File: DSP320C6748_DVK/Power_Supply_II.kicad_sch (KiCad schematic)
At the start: 46 parts, among them IC8 TPS650250RHBR

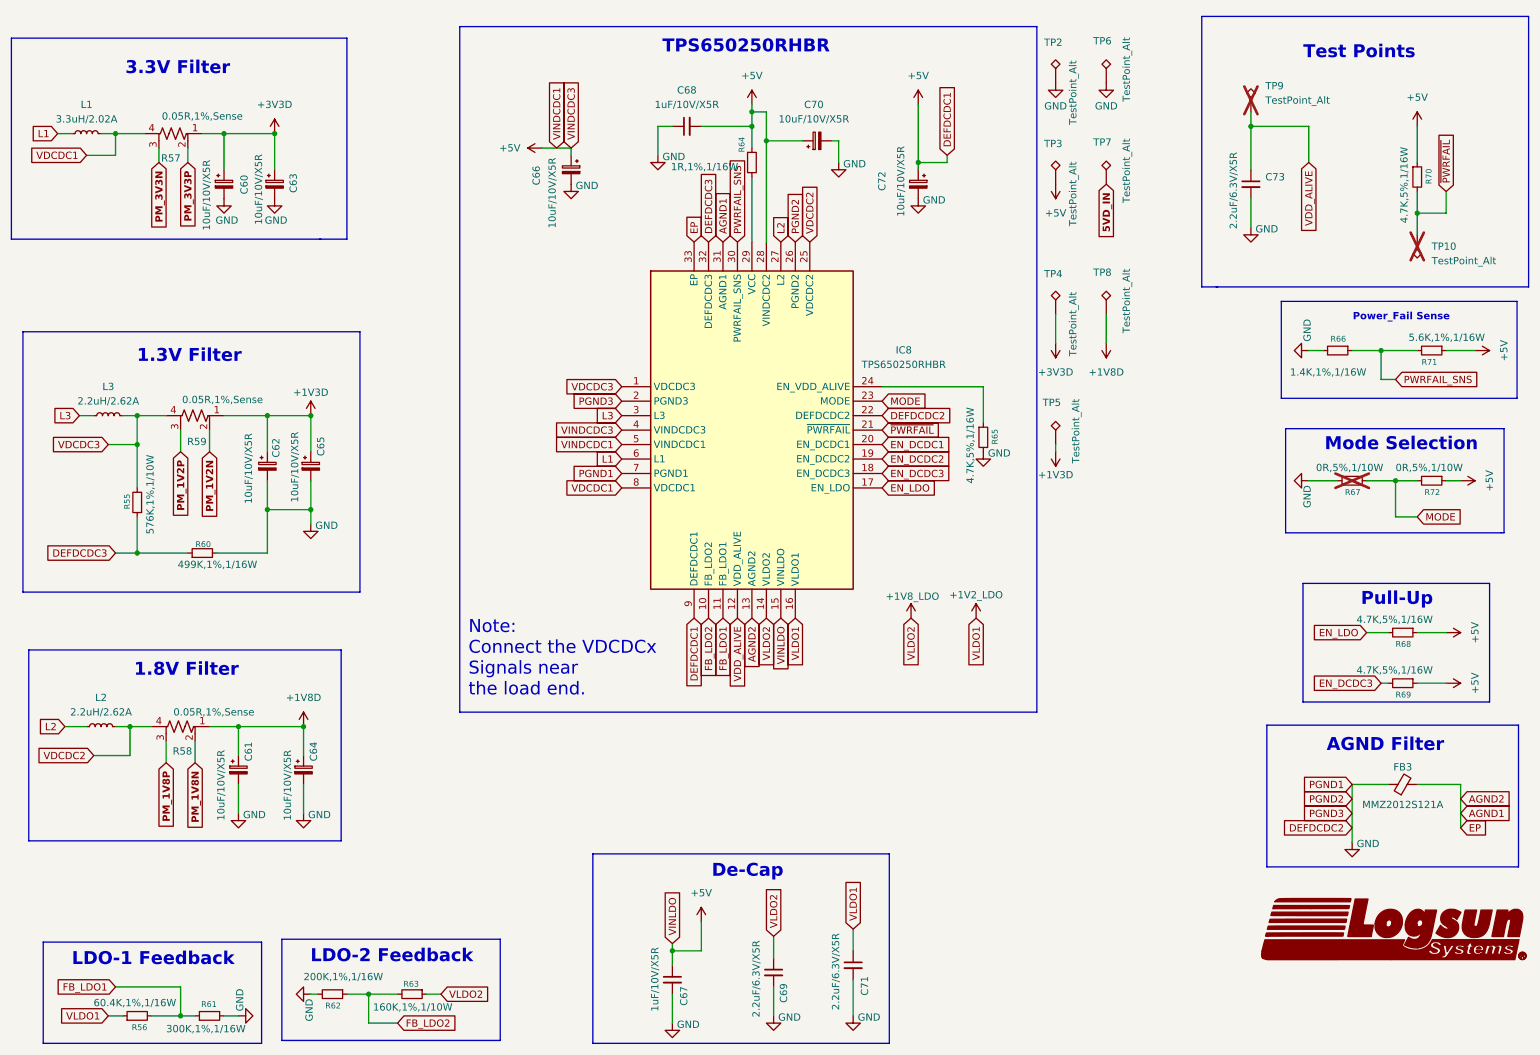
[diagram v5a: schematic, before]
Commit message: Scheamtic Re-annotation done, Some footprints assigned
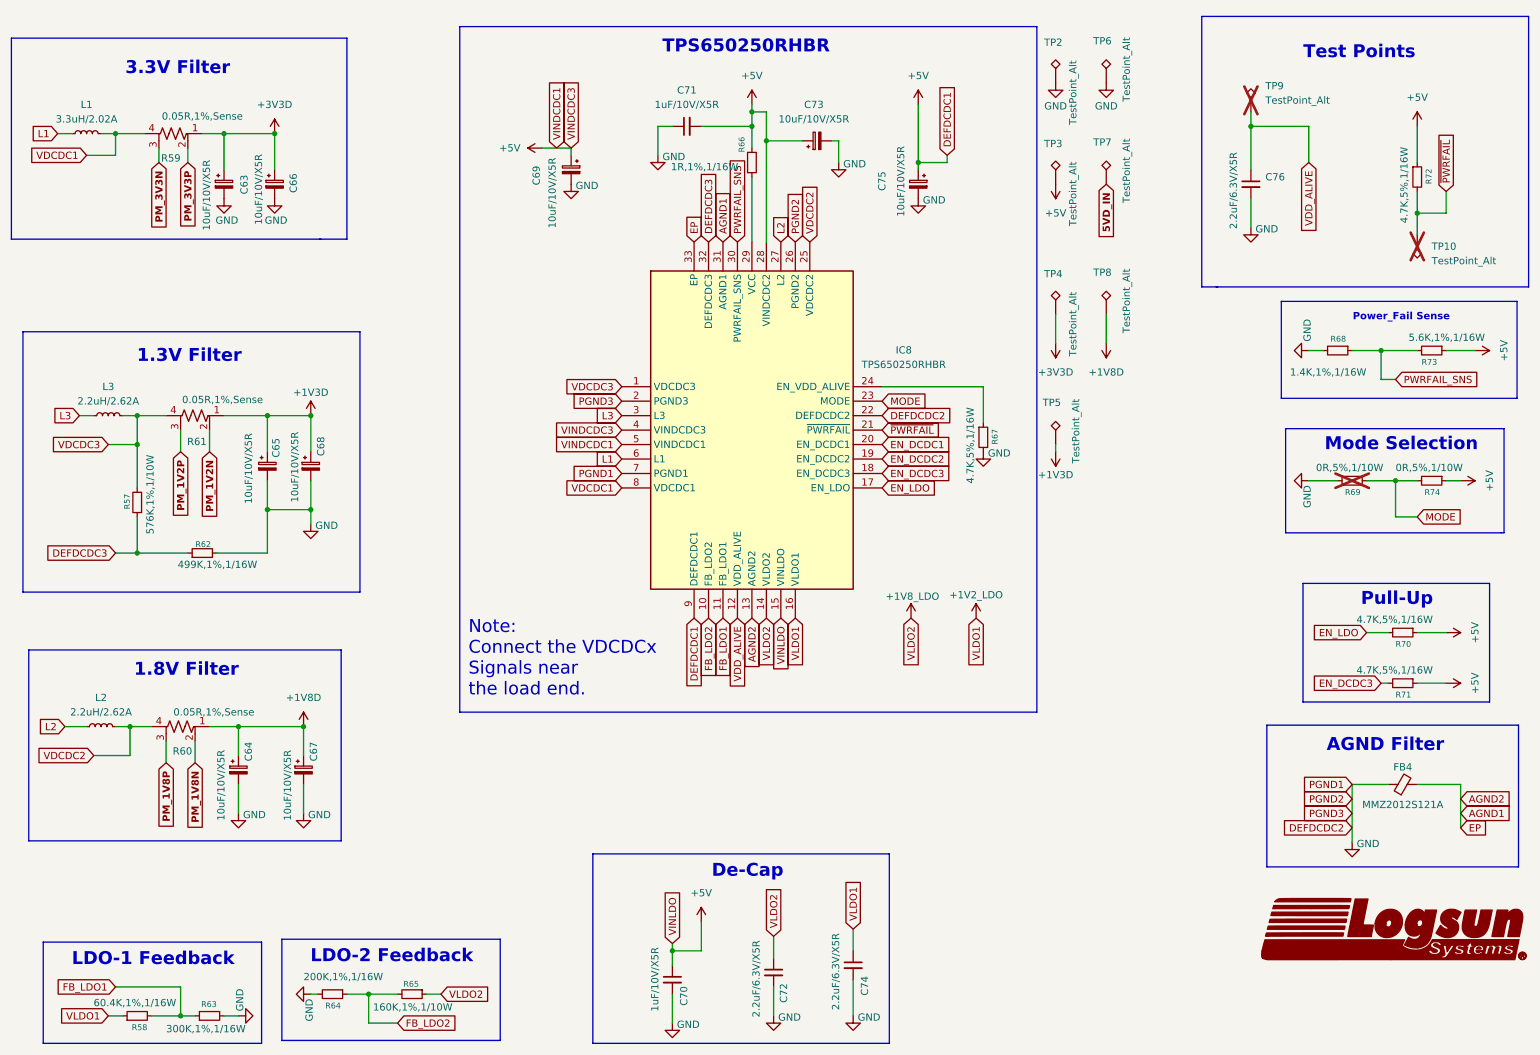
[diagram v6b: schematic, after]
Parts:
- C63: renamed from C60; footprint (none) -> Capacitor_SMD:C_0603_1608Metric_Pad1.08x0.95mm_HandSolder
- C64: renamed from C61; footprint (none) -> Capacitor_SMD:C_0603_1608Metric_Pad1.08x0.95mm_HandSolder
- C65: renamed from C62; footprint (none) -> Capacitor_SMD:C_0603_1608Metric_Pad1.08x0.95mm_HandSolder
- C66: renamed from C63; footprint (none) -> Capacitor_SMD:C_0603_1608Metric_Pad1.08x0.95mm_HandSolder
- C67: renamed from C64; footprint (none) -> Capacitor_SMD:C_0603_1608Metric_Pad1.08x0.95mm_HandSolder
- C68: renamed from C65; footprint (none) -> Capacitor_SMD:C_0603_1608Metric_Pad1.08x0.95mm_HandSolder
- C69: renamed from C66; footprint (none) -> Capacitor_SMD:C_0603_1608Metric_Pad1.08x0.95mm_HandSolder
- C70: renamed from C67; footprint (none) -> Capacitor_SMD:C_0603_1608Metric_Pad1.08x0.95mm_HandSolder
- C71: renamed from C68; footprint (none) -> Capacitor_SMD:C_0603_1608Metric_Pad1.08x0.95mm_HandSolder
- C72: renamed from C69; footprint (none) -> Capacitor_SMD:C_0603_1608Metric_Pad1.08x0.95mm_HandSolder
- C73: renamed from C70; footprint (none) -> Capacitor_SMD:C_0603_1608Metric_Pad1.08x0.95mm_HandSolder
- C74: renamed from C71; footprint (none) -> Capacitor_SMD:C_0603_1608Metric_Pad1.08x0.95mm_HandSolder
- C75: renamed from C72; footprint (none) -> Capacitor_SMD:C_0603_1608Metric_Pad1.08x0.95mm_HandSolder
- C76: renamed from C73; footprint (none) -> Capacitor_SMD:C_0603_1608Metric_Pad1.08x0.95mm_HandSolder
- FB4: renamed from FB3; footprint (none) -> Inductor_SMD:L_0805_2012Metric_Pad1.05x1.20mm_HandSolder
- R57: renamed from R55; footprint (none) -> Resistor_SMD:R_0603_1608Metric_Pad0.98x0.95mm_HandSolder
- R58: renamed from R56; footprint (none) -> Resistor_SMD:R_0603_1608Metric_Pad0.98x0.95mm_HandSolder
- R59: renamed from R57; footprint (none) -> Resistor_SMD:R_0603_1608Metric_Pad0.98x0.95mm_HandSolder
- R60: renamed from R58; footprint (none) -> Resistor_SMD:R_0603_1608Metric_Pad0.98x0.95mm_HandSolder
- R61: renamed from R59; footprint (none) -> Resistor_SMD:R_0603_1608Metric_Pad0.98x0.95mm_HandSolder
- R62: renamed from R60; footprint (none) -> Resistor_SMD:R_0603_1608Metric_Pad0.98x0.95mm_HandSolder
- R63: renamed from R61; footprint (none) -> Resistor_SMD:R_0603_1608Metric_Pad0.98x0.95mm_HandSolder
- R64: renamed from R62; footprint (none) -> Resistor_SMD:R_0603_1608Metric_Pad0.98x0.95mm_HandSolder
- R65: renamed from R63; footprint (none) -> Resistor_SMD:R_0603_1608Metric_Pad0.98x0.95mm_HandSolder
- R66: renamed from R64; footprint (none) -> Resistor_SMD:R_0603_1608Metric_Pad0.98x0.95mm_HandSolder
- R67: renamed from R65; footprint (none) -> Resistor_SMD:R_0603_1608Metric_Pad0.98x0.95mm_HandSolder
- R68: renamed from R66; footprint (none) -> Resistor_SMD:R_0603_1608Metric_Pad0.98x0.95mm_HandSolder
- R69: renamed from R67; footprint (none) -> Resistor_SMD:R_0603_1608Metric_Pad0.98x0.95mm_HandSolder
- R70: renamed from R68; footprint (none) -> Resistor_SMD:R_0603_1608Metric_Pad0.98x0.95mm_HandSolder
- R71: renamed from R69; footprint (none) -> Resistor_SMD:R_0603_1608Metric_Pad0.98x0.95mm_HandSolder
- R72: renamed from R70; footprint (none) -> Resistor_SMD:R_0603_1608Metric_Pad0.98x0.95mm_HandSolder
- R73: renamed from R71; footprint (none) -> Resistor_SMD:R_0603_1608Metric_Pad0.98x0.95mm_HandSolder
- R74: renamed from R72; footprint (none) -> Resistor_SMD:R_0603_1608Metric_Pad0.98x0.95mm_HandSolder
- TP10, TP2, TP3, TP4, TP5, TP6, TP7, TP8, TP9: footprint (none) -> TestPoint:TestPoint_Pad_D3.0mm
